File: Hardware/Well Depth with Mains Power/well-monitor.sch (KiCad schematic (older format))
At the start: 33 parts, among them J1 Screw_Terminal_01x04, J2 Screw_Terminal_01x04, J3 Screw_Terminal_01x04, J4 ISP Header, J5 Screw_Terminal_01x02, J6 USB_B_Micro, J7 Micro_SD_Card, J8 SENSOR, SW1 SW_Push, U1 ATmega328P-PU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

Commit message: First pass routing and DRC/ERC pass
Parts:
- removed U5: MCP7940N-xSN, symbol Timer:MCP7940N-xSN
- added C10, C11, C12, C8, C9: 100n, Capacitor_SMD:C_0603_1608Metric, symbol Device:C_Small
- added C13, C14: 10p, Capacitor_SMD:C_0603_1608Metric, symbol Device:C_Small
- added C15: 1u, Capacitor_SMD:C_1206_3216Metric, symbol Device:C_Small
- added C16: 68u, Capacitor_THT:CP_Radial_D10.0mm_P5.00mm, symbol Device:CP1_Small
- added D5: SMBJ30A, Diode_SMD:D_SMB, symbol Device:D_Zener_Small
- added H1, H2, H3, H4: MountingHole, MountingHole:MountingHole_3.2mm_M3, symbol Mechanical:MountingHole
- added R6: 12, Resistor_SMD:R_1206_3216Metric, symbol Device:R
- added RV1: S10K350, Varistor:RV_Disc_D12mm_W5.4mm_P7.5mm, symbol Device:Varistor
- added U5: MCP7940N-xMS, Package_SO:TSSOP-8_4.4x3mm_P0.65mm, symbol Timer:MCP7940N-xMS
- added Y2: 16Meg, Crystal:Crystal_HC49-U_Vertical, symbol Device:Crystal_Small
- BT1: footprint (none) -> well-monitor:BatteryHolder_Keystone_3002_1x2032
- C1, C2, C3, C4, C5, C6, C7: footprint (none) -> Capacitor_SMD:C_0603_1608Metric
- D1, D2: value D_Schottky_Small -> CUS10S30; footprint (none) -> Diode_SMD:D_SOD-323
- D3: footprint (none) -> Diode_SMD:D_SOD-123
- D4: footprint (none) -> LED_SMD:LED_0603_1608Metric
- F1: value Automotive Fuse -> 1; footprint (none) -> Fuse:Fuse_1206_3216Metric
- J1, J2, J3: footprint (none) -> well-monitor:TerminalBlock_Phoenix_PT-1,5-4-5.0-H_1x04_P5.00mm_Horizontal
- J4: footprint (none) -> Connector_PinHeader_2.54mm:PinHeader_2x03_P2.54mm_Vertical
- J5, J8: footprint (none) -> well-monitor:TerminalBlock_Phoenix_PT-1,5-2-5.0-H_1x02_P5.00mm_Horizontal
- J6: footprint (none) -> well-monitor:USB_Micro-B_GCT_USB3076-30-A
- J7: footprint (none) -> well-monitor:MEM2051-00-195-00-A
- R1, R2, R3, R4, R5: footprint (none) -> Resistor_SMD:R_0603_1608Metric
- SW1: footprint (none) -> well-monitor:PTS636-SP43-LFS
- U2: footprint (none) -> well-monitor:PSK-5D-24
- Y1: footprint (none) -> Crystal:Crystal_SMD_MicroCrystal_CM9V-T1A-2Pin_1.6x1.0mm
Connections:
- net +24V: now also C15.1, C16.1, D5.1 (K)
- net +3V3: now also C10.2, C11.1, C12.2, C8.2, C9.2, U5.8 (VCC)
- net GND: now also C10.1, C11.2, C12.1, C13.1, C14.2, C15.2, C16.2, C8.1, C9.1, D5.2 (A), U5.4 (VSS)
- net GPIO_2: now also U5.5 (SDA)
- net GPIO_3: now also U5.6 (SCL)
- net GPIO_4: now also U1.5 (PD3); no longer U1.4 (PD2)
- net GPIO_5: now also U1.6 (PD4); no longer U1.5 (PD3)
- net GPIO_6: now also U1.11 (PD5); no longer U1.6 (PD4)
- net GPIO_7: now also U1.12 (PD6); no longer U1.11 (PD5)
- net RTC_MFP: now also U1.4 (PD2), U5.7 (MFP); no longer U1.24 (PC1)
- net SD_~DET: now also U1.13 (PD7); no longer U1.12 (PD6)
- net at U2.1 (AC(N)): now also J5.2 (Pin_2), RV1.1; no longer F1.1
- net at U2.2 (AC(L)): now also R6.2; no longer J5.2 (Pin_2)
- net at C4.2, Y1.1: now also U5.1 (X1)
- net at C5.1, Y1.2: now also U5.2 (X2)
- net at BT1.1 (+): now also U5.3 (VBAT)
- net at U1.10 (XTAL2/PB7): now also C14.1, Y2.2
- net at U1.9 (XTAL1/PB6): now also C13.2, Y2.1
- new net: F1.1, R6.1, RV1.2
- no-connect marks 28 -> 26
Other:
- moved on the sheet: BT1, C2, C3, C4, C5, D1, D2, D3, F1, J1, J2, J3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

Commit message: Received hardware, started implementing software
Arduino IDE compatibility works, and SD card data logging has been tested and is functional.
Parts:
- R6: footprint Resistor_SMD:R_1206_3216Metric -> Resistor_THT:R_Axial_DIN0617_L17.0mm_D6.0mm_P7.62mm_Vertical
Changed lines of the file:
@@
 F 0 "R6" V 2000 1500 50  0000 C CNN
 F 1 "12" V 1900 1500 50  0000 C CNN
-F 2 "Resistor_SMD:R_1206_3216Metric" V 1730 1500 50  0001 C CNN
+F 2 "Resistor_THT:R_Axial_DIN0617_L17.0mm_D6.0mm_P7.62mm_Vertical" V 1730 1500 50  0001 C CNN
 F 3 "~" H 1800 1500 50  0001 C CNN
 	1    1800 1500

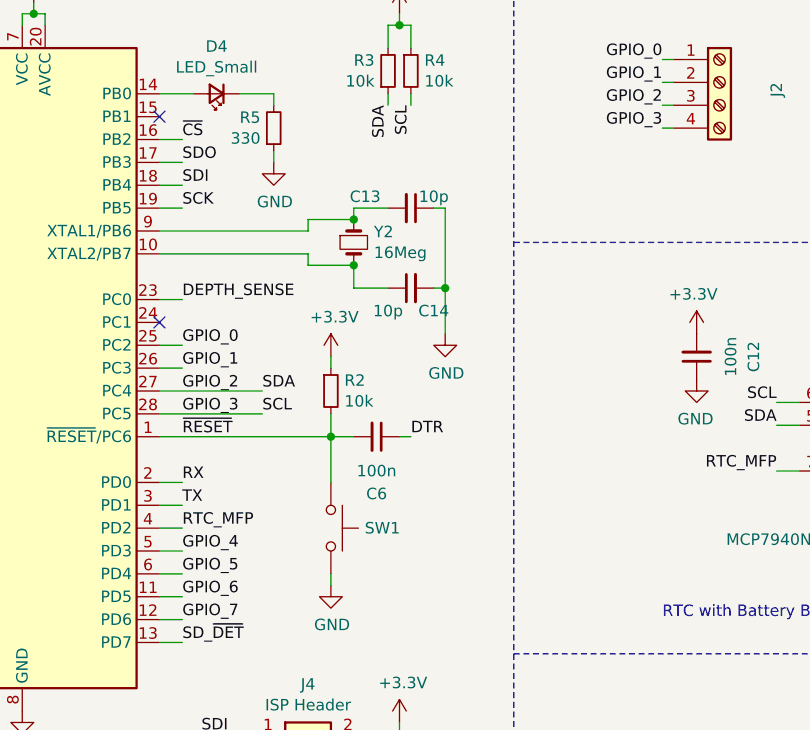
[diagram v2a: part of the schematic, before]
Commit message: V1 (Fix issues with V0)
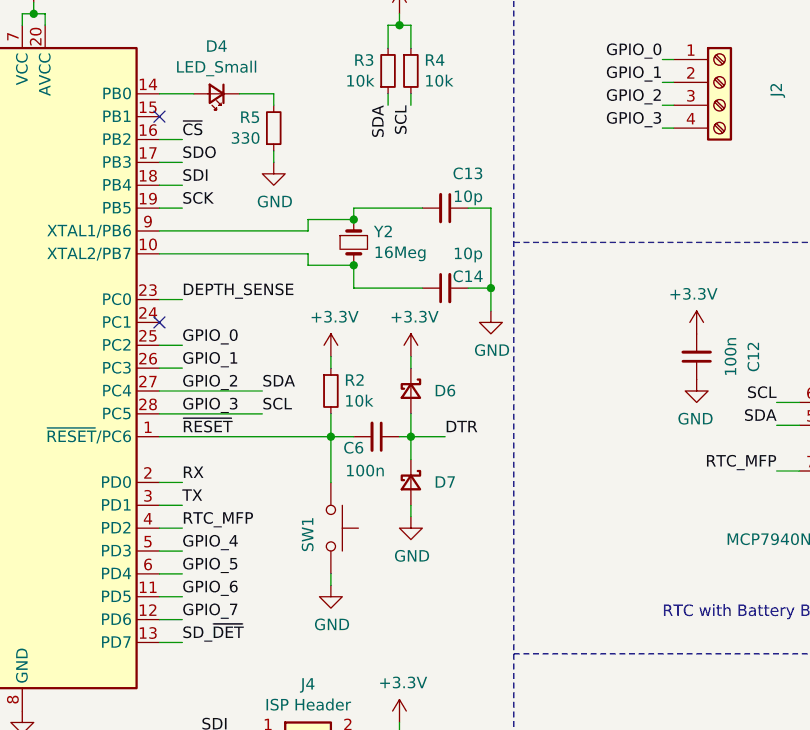
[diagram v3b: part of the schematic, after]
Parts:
- added D6, D7: CUS10S30, Diode_SMD:D_SOD-323, symbol Device:D_Schottky_Small
- R6: footprint Resistor_THT:R_Axial_DIN0617_L17.0mm_D6.0mm_P7.62mm_Vertical -> Resistor_THT:R_Axial_DIN0614_L14.3mm_D5.7mm_P20.32mm_Horizontal
- U5: footprint Package_SO:TSSOP-8_4.4x3mm_P0.65mm -> Package_SO:MSOP-8_3x3mm_P0.65mm
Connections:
- net +3V3: now also D6.1 (K)
- net DTR: now also D6.2 (A), D7.1 (K)
- net GND: now also D7.2 (A)
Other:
- moved on the sheet: C13, C14
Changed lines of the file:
@@
 Text Notes 3800 6050 0    50   ~ 0
 ATMEGA328P/Arduino Core
-Text Label 6750 4250 0    50   ~ 0
+Text Label 6900 4250 0    50   ~ 0
 DTR
 $Comp
@@
 U 1 1 619C4E76
 P 6600 4250
-F 0 "C6" V 6850 4250 50  0000 C CNN
-F 1 "100n" V 6750 4250 50  0000 C CNN
+F 0 "C6" V 6650 4150 50  0000 C CNN
+F 1 "100n" V 6750 4200 50  0000 C CNN
 F 2 "Capacitor_SMD:C_0603_1608Metric" H 6600 4250 50  0001 C CNN
 F 3 "~" H 6600 4250 50  0001 C CNN
@@
 U 1 1 619E0A30
 P 6400 4650
-F 0 "SW1" V 6400 4798 50  0000 L CNN
+F 0 "SW1" H 6350 4550 50  0000 L CNN
 F 1 "SW_Push" V 6445 4798 50  0001 L CNN
 F 2 "well-monitor:PTS636-SP43-LFS" H 6400 4850 50  0001 C CNN
@@
 L Device:C_Small C13
 U 1 1 6185AB7E
-P 6750 3250
-F 0 "C13" V 6700 3050 50  0000 C CNN
-F 1 "10p" V 6700 3350 50  0000 C CNN
-F 2 "Capacitor_SMD:C_0603_1608Metric" H 6750 3250 50  0001 C CNN
-F 3 "~" H 6750 3250 50  0001 C CNN
-	1    6750 3250
+P 6900 3250
+F 0 "C13" V 6750 3350 50  0000 C CNN
+F 1 "10p" V 6850 3350 50  0000 C CNN
+F 2 "Capacitor_SMD:C_0603_1608Metric" H 6900 3250 50  0001 C CNN
+F 3 "~" H 6900 3250 50  0001 C CNN
+	1    6900 3250
 	0    1    1    0
 $EndComp
@@
 L Device:C_Small C14
 U 1 1 6185AB84
-P 6750 3600
-F 0 "C14" V 6650 3500 50  0000 C CNN
-F 1 "10p" V 6650 3700 50  0000 C CNN
-F 2 "Capacitor_SMD:C_0603_1608Metric" H 6750 3600 50  0001 C CNN
-F 3 "~" H 6750 3600 50  0001 C CNN
-	1    6750 3600
+P 6900 3600
+F 0 "C14" V 6950 3500 50  0000 C CNN
+F 1 "10p" V 7050 3500 50  0000 C CNN
+F 2 "Capacitor_SMD:C_0603_1608Metric" H 6900 3600 50  0001 C CNN
+F 3 "~" H 6900 3600 50  0001 C CNN
+	1    6900 3600
 	0    -1   -1   0
 $EndComp
@@
 L power:GND #PWR0135
 U 1 1 6185AB8A
-P 6900 3800
-F 0 "#PWR0135" H 6900 3550 50  0001 C CNN
-F 1 "GND" H 6905 3627 50  0000 C CNN
-F 2 "" H 6900 3800 50  0001 C CNN
-F 3 "" H 6900 3800 50  0001 C CNN
-	1    6900 3800
-	1    0    0    -1
-$EndComp
-Wire Wire Line
-	6900 3800 6900 3600
-Wire Wire Line
-	6900 3250 6850 3250
-Wire Wire Line
-	6850 3600 6900 3600
-Connection ~ 6900 3600
-Wire Wire Line
-	6900 3600 6900 3250
-Wire Wire Line
-	6650 3600 6500 3600
+P 7100 3700
+F 0 "#PWR0135" H 7100 3450 50  0001 C CNN
+F 1 "GND" H 7105 3527 50  0000 C CNN
+F 2 "" H 7100 3700 50  0001 C CNN
+F 3 "" H 7100 3700 50  0001 C CNN
+	1    7100 3700
+	1    0    0    -1
+$EndComp
+Wire Wire Line
+	7100 3700 7100 3600
+Wire Wire Line
+	7100 3250 7000 3250
+Wire Wire Line
+	7000 3600 7100 3600
+Connection ~ 7100 3600
+Wire Wire Line
+	7100 3600 7100 3250
+Wire Wire Line
+	6800 3600 6500 3600
 Wire Wire Line
 	6500 3600 6500 3500
 Connection ~ 6500 3500
 Wire Wire Line
-	6650 3250 6500 3250
+	6800 3250 6500 3250
 Wire Wire Line
 	6500 3250 6500 3300
@@
 F 0 "U5" H 9100 3950 50  0000 C CNN
 F 1 "MCP7940N-xMS" H 8400 3900 50  0000 C CNN
-F 2 "Package_SO:TSSOP-8_4.4x3mm_P0.65mm" H 8850 4300 50  0001 C CNN
+F 2 "Package_SO:MSOP-8_3x3mm_P0.65mm" H 8850 4300 50  0001 C CNN
 F 3 "http://ww1.microchip.com/downloads/en/DeviceDoc/20005010F.pdf" H 8850 4300 50  0001 C CNN
 	1    8850 4300
@@
 F 0 "R6" V 2000 1500 50  0000 C CNN
 F 1 "12" V 1900 1500 50  0000 C CNN
-F 2 "Resistor_THT:R_Axial_DIN0617_L17.0mm_D6.0mm_P7.62mm_Vertical" V 1730 1500 50  0001 C CNN
+F 2 "Resistor_THT:R_Axial_DIN0614_L14.3mm_D5.7mm_P20.32mm_Horizontal" V 1730 1500 50  0001 C CNN
 F 3 "~" H 1800 1500 50  0001 C CNN
 	1    1800 1500
@@
 Wire Notes Line
 	7200 5200 10500 5200
+$Comp
+L Device:D_Schottky_Small D6
+U 1 1 618D3BC4
+P 6750 4050
+F 0 "D6" V 6750 4200 50  0000 C CNN
+F 1 "CUS10S30" H 6750 3934 50  0001 C CNN
+F 2 "Diode_SMD:D_SOD-323" V 6750 4050 50  0001 C CNN
+F 3 "~" V 6750 4050 50  0001 C CNN
+	1    6750 4050
+	0    1    1    0
+$EndComp
+$Comp
+L Device:D_Schottky_Small D7
+U 1 1 618D46D0
+P 6750 4450
+F 0 "D7" V 6750 4600 50  0000 C CNN
+F 1 "CUS10S30" H 6800 4600 50  0001 C CNN
+F 2 "Diode_SMD:D_SOD-323" V 6750 4450 50  0001 C CNN
+F 3 "~" V 6750 4450 50  0001 C CNN
+	1    6750 4450
+	0    1    1    0
+$EndComp
+$Comp
+L power:+3.3V #PWR012
+U 1 1 618D4D03
+P 6750 3900
+F 0 "#PWR012" H 6750 3750 50  0001 C CNN
+F 1 "+3.3V" H 6765 4073 50  0000 C CNN
+F 2 "" H 6750 3900 50  0001 C CNN
+F 3 "" H 6750 3900 50  0001 C CNN
+	1    6750 3900
+	1    0    0    -1
+$EndComp
+Wire Wire Line
+	6750 3900 6750 3950
+Wire Wire Line
+	6750 4150 6750 4250
+Wire Wire Line
+	6750 4250 6750 4350
+Connection ~ 6750 4250
+$Comp
+L power:GND #PWR013
+U 1 1 61918E6C
+P 6750 4600
+F 0 "#PWR013" H 6750 4350 50  0001 C CNN
+F 1 "GND" H 6755 4427 50  0000 C CNN
+F 2 "" H 6750 4600 50  0001 C CNN
+F 3 "" H 6750 4600 50  0001 C CNN
+	1    6750 4600
+	1    0    0    -1
+$EndComp
+Wire Wire Line
+	6750 4600 6750 4550
+Wire Wire Line
+	6900 4250 6750 4250
 $EndSCHEMATC

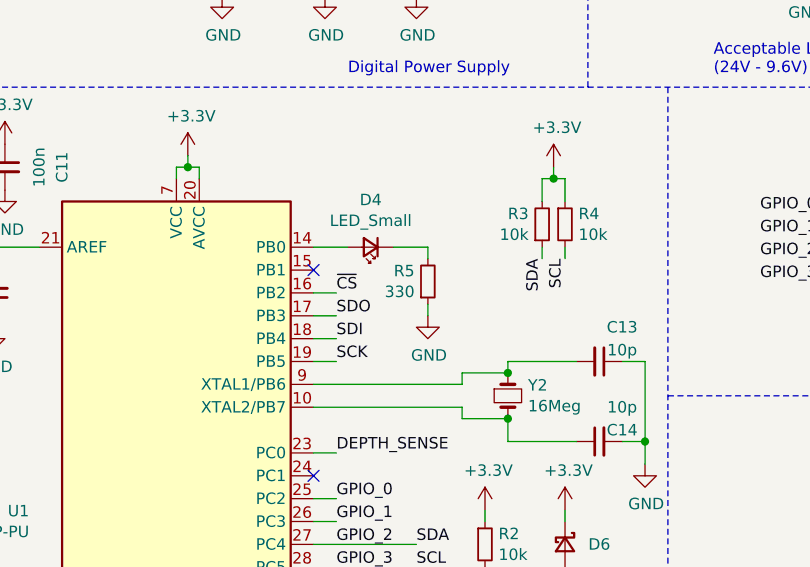
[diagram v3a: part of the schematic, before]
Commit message: Well Monitor: Update to newest KiCAD version
Also updated CAM files
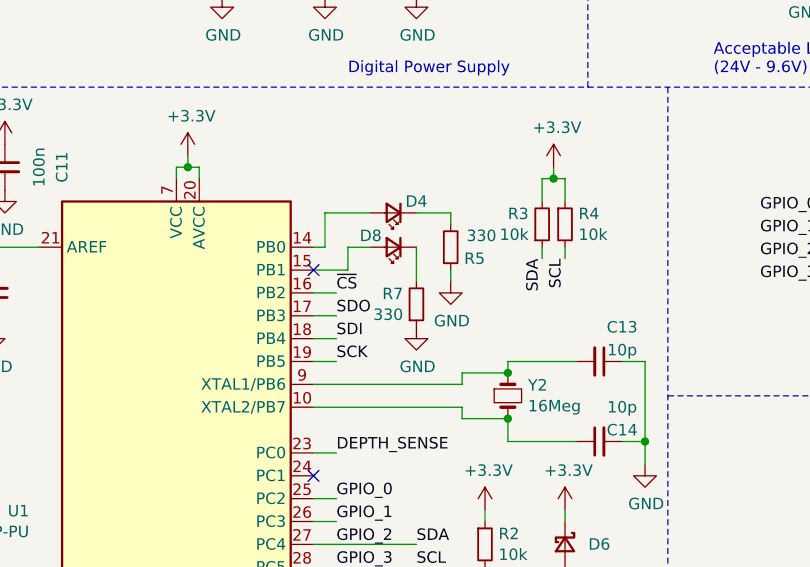
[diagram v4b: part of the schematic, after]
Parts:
- added D8: LED_Small, LED_SMD:LED_0603_1608Metric, symbol Device:LED_Small
- added R7: 330, Resistor_SMD:R_0603_1608Metric, symbol Device:R_Small
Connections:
- net GND: now also R7.1
- net at U1.15 (PB1): now also D8.2 (A)
- new net: D8.1 (K), R7.2
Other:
- moved on the sheet: D4, R5
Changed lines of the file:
@@
 L Device:LED_Small D4
 U 1 1 61A4547F
-P 5900 2750
-F 0 "D4" H 5900 2543 50  0000 C CNN
-F 1 "LED_Small" H 5900 2634 50  0000 C CNN
-F 2 "LED_SMD:LED_0603_1608Metric" V 5900 2750 50  0001 C CNN
-F 3 "~" V 5900 2750 50  0001 C CNN
-	1    5900 2750
+P 6000 2600
+F 0 "D4" H 5900 2550 50  0000 C CNN
+F 1 "LED_Small" H 6000 2484 50  0001 C CNN
+F 2 "LED_SMD:LED_0603_1608Metric" V 6000 2600 50  0001 C CNN
+F 3 "~" V 6000 2600 50  0001 C CNN
+	1    6000 2600
 	-1   0    0    1
 $EndComp
@@
 L Device:R_Small R5
 U 1 1 61A45DAC
-P 6150 2900
-F 0 "R5" H 6092 2854 50  0000 R CNN
-F 1 "330" H 6092 2945 50  0000 R CNN
-F 2 "Resistor_SMD:R_0603_1608Metric" H 6150 2900 50  0001 C CNN
-F 3 "~" H 6150 2900 50  0001 C CNN
-	1    6150 2900
+P 6250 2750
+F 0 "R5" H 6400 2800 50  0000 R CNN
+F 1 "330" H 6450 2700 50  0000 R CNN
+F 2 "Resistor_SMD:R_0603_1608Metric" H 6250 2750 50  0001 C CNN
+F 3 "~" H 6250 2750 50  0001 C CNN
+	1    6250 2750
 	1    0    0    1
 $EndComp
@@
 L power:GND #PWR01
 U 1 1 61A46644
-P 6150 3050
-F 0 "#PWR01" H 6150 2800 50  0001 C CNN
-F 1 "GND" H 6155 2877 50  0000 C CNN
-F 2 "" H 6150 3050 50  0001 C CNN
-F 3 "" H 6150 3050 50  0001 C CNN
-	1    6150 3050
-	1    0    0    -1
-$EndComp
-Wire Wire Line
-	6150 3050 6150 3000
-Wire Wire Line
-	6150 2800 6150 2750
-Wire Wire Line
-	6150 2750 6000 2750
-Wire Wire Line
-	5800 2750 5650 2750
+P 6250 2900
+F 0 "#PWR01" H 6250 2650 50  0001 C CNN
+F 1 "GND" H 6255 2727 50  0000 C CNN
+F 2 "" H 6250 2900 50  0001 C CNN
+F 3 "" H 6250 2900 50  0001 C CNN
+	1    6250 2900
+	1    0    0    -1
+$EndComp
+Wire Wire Line
+	6250 2900 6250 2850
+Wire Wire Line
+	6250 2650 6250 2600
+Wire Wire Line
+	6250 2600 6100 2600
 NoConn ~ 5650 3750
 Wire Wire Line
@@
 Wire Wire Line
 	6900 4250 6750 4250
+$Comp
+L Device:LED_Small D8
+U 1 1 6197A786
+P 6000 2750
+F 0 "D8" H 6100 2700 50  0000 C CNN
+F 1 "LED_Small" H 6000 2634 50  0001 C CNN
+F 2 "LED_SMD:LED_0603_1608Metric" V 6000 2750 50  0001 C CNN
+F 3 "~" V 6000 2750 50  0001 C CNN
+	1    6000 2750
+	-1   0    0    1
+$EndComp
+Wire Wire Line
+	5900 2600 5700 2600
+Wire Wire Line
+	5700 2600 5700 2750
+Wire Wire Line
+	5700 2750 5650 2750
+Wire Wire Line
+	5650 2850 5800 2850
+Wire Wire Line
+	5800 2850 5800 2750
+$Comp
+L Device:R_Small R7
+U 1 1 6199A90E
+P 6100 3000
+F 0 "R7" H 6042 2954 50  0000 R CNN
+F 1 "330" H 6042 3045 50  0000 R CNN
+F 2 "Resistor_SMD:R_0603_1608Metric" H 6100 3000 50  0001 C CNN
+F 3 "~" H 6100 3000 50  0001 C CNN
+	1    6100 3000
+	1    0    0    1
+$EndComp
+$Comp
+L power:GND #PWR014
+U 1 1 6199AB93
+P 6100 3100
+F 0 "#PWR014" H 6100 2850 50  0001 C CNN
+F 1 "GND" H 6105 2927 50  0000 C CNN
+F 2 "" H 6100 3100 50  0001 C CNN
+F 3 "" H 6100 3100 50  0001 C CNN
+	1    6100 3100
+	1    0    0    -1
+$EndComp
+Wire Wire Line
+	5900 2750 5800 2750
+Wire Wire Line
+	6100 2750 6100 2900
 $EndSCHEMATC
